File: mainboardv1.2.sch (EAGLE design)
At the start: 128 parts, among them IC1 LM2596S, IC2 TDA2822D, IC3 MCP2562P, IC4 STM32F103RBT6, IC5 MIC2288YD5, IC6 ULN2003AD, IC7 LM2901, IC8 REG1117, IC9 SN74LVC1G10, Q1 8MHz

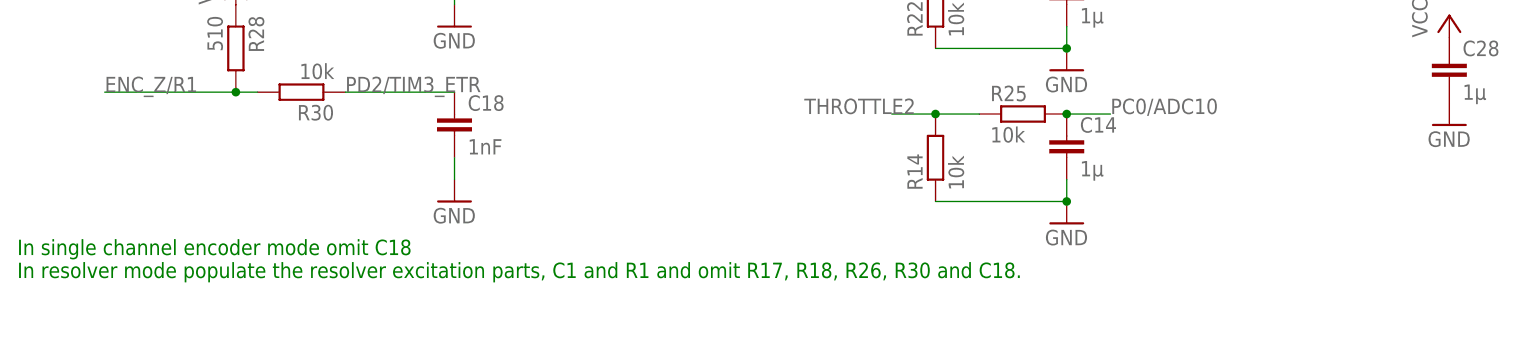
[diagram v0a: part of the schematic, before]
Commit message: Small changed for compatibility with JLCPCBs parts library
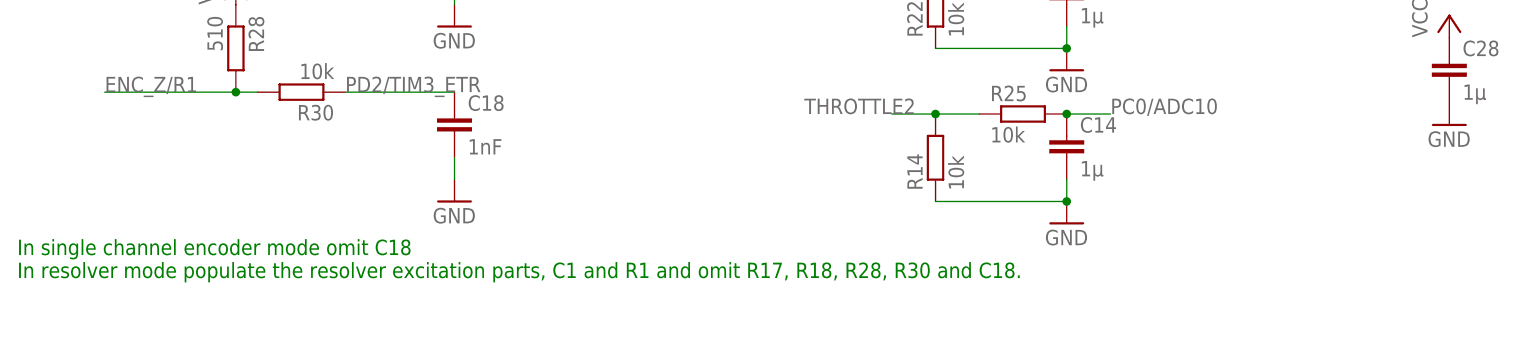
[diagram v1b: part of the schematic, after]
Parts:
- L4: device rcl:L-EUL2012C -> rcl:L-EUL2825P
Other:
- note added: "In single channel encoder mode omit C18 In resolver mode populate the resolver excitation parts, C1 and R1 and omit R17, R18, R28, R30 and C18."
- note removed: "In single channel encoder mode omit C18 In resolver mode populate the resolver excitation parts, C1 and R1 and omit R17, R18, R26, R30 and C18."
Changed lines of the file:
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@@
 <grid distance="0.1" unitdist="inch" unit="inch" style="lines" multiple="1" display="no" altdistance="0.01" altunitdist="inch" altunit="inch"/>
 <layers>
-<layer number="1" name="Top" color="12" fill="1" visible="no" active="no"/>
-<layer number="16" name="Bottom" color="1" fill="1" visible="no" active="no"/>
-<layer number="17" name="Pads" color="2" fill="1" visible="no" active="no"/>
-<layer number="18" name="Vias" color="2" fill="1" visible="no" active="no"/>
-<layer number="19" name="Unrouted" color="15" fill="1" visible="no" active="no"/>
-<layer number="20" name="Dimension" color="15" fill="1" visible="no" active="no"/>
-<layer number="21" name="tPlace" color="7" fill="1" visible="no" active="no"/>
-<layer number="22" name="bPlace" color="7" fill="1" visible="no" active="no"/>
-<layer number="23" name="tOrigins" color="15" fill="1" visible="no" active="no"/>
-<layer number="24" name="bOrigins" color="15" fill="1" visible="no" active="no"/>
-<layer number="25" name="tNames" color="7" fill="1" visible="no" active="no"/>
-<layer number="26" name="bNames" color="7" fill="1" visible="no" active="no"/>
-<layer number="27" name="tValues" color="7" fill="1" visible="no" active="no"/>
-<layer number="28" name="bValues" color="7" fill="1" visible="no" active="no"/>
+<layer number="1" name="Top" color="12" fill="1" visible="yes" active="no"/>
+<layer number="16" name="Bottom" color="1" fill="1" visible="yes" active="no"/>
+<layer number="17" name="Pads" color="2" fill="1" visible="yes" active="no"/>
+<layer number="18" name="Vias" color="2" fill="1" visible="yes" active="no"/>
+<layer number="19" name="Unrouted" color="15" fill="1" visible="yes" active="no"/>
+<layer number="20" name="Dimension" color="15" fill="1" visible="yes" active="no"/>
+<layer number="21" name="tPlace" color="7" fill="1" visible="yes" active="no"/>
+<layer number="22" name="bPlace" color="7" fill="1" visible="yes" active="no"/>
+<layer number="23" name="tOrigins" color="15" fill="1" visible="yes" active="no"/>
+<layer number="24" name="bOrigins" color="15" fill="1" visible="yes" active="no"/>
+<layer number="25" name="tNames" color="7" fill="1" visible="yes" active="no"/>
+<layer number="26" name="bNames" color="7" fill="1" visible="yes" active="no"/>
+<layer number="27" name="tValues" color="7" fill="1" visible="yes" active="no"/>
+<layer number="28" name="bValues" color="7" fill="1" visible="yes" active="no"/>
 <layer number="29" name="tStop" color="7" fill="3" visible="no" active="no"/>
 <layer number="30" name="bStop" color="7" fill="6" visible="no" active="no"/>
@@
 <layer number="35" name="tGlue" color="7" fill="4" visible="no" active="no"/>
 <layer number="36" name="bGlue" color="7" fill="5" visible="no" active="no"/>
-<layer number="37" name="tTest" color="7" fill="1" visible="no" active="no"/>
-<layer number="38" name="bTest" color="7" fill="1" visible="no" active="no"/>
+<layer number="37" name="tTest" color="7" fill="1" visible="yes" active="no"/>
+<layer number="38" name="bTest" color="7" fill="1" visible="yes" active="no"/>
 <layer number="39" name="tKeepout" color="4" fill="11" visible="no" active="no"/>
 <layer number="40" name="bKeepout" color="1" fill="11" visible="no" active="no"/>
@@
 <layer number="44" name="Drills" color="7" fill="1" visible="no" active="no"/>
 <layer number="45" name="Holes" color="7" fill="1" visible="no" active="no"/>
-<layer number="46" name="Milling" color="3" fill="1" visible="no" active="no"/>
-<layer number="47" name="Measures" color="7" fill="1" visible="no" active="no"/>
-<layer number="48" name="Document" color="7" fill="1" visible="no" active="no"/>
-<layer number="49" name="Reference" color="7" fill="1" visible="no" active="no"/>
-<layer number="50" name="dxf" color="7" fill="1" visible="no" active="no"/>
-<layer number="51" name="tDocu" color="7" fill="1" visible="no" active="no"/>
-<layer number="52" name="bDocu" color="7" fill="1" visible="no" active="no"/>
-<layer number="53" name="tGND_GNDA" color="7" fill="9" visible="no" active="no"/>
-<layer number="54" name="bGND_GNDA" color="1" fill="9" visible="no" active="no"/>
-<layer number="56" name="wert" color="7" fill="1" visible="no" active="no"/>
-<layer number="57" name="tCAD" color="7" fill="1" visible="no" active="no"/>
+<layer number="46" name="Milling" color="3" fill="1" visible="yes" active="no"/>
+<layer number="47" name="Measures" color="7" fill="1" visible="yes" active="no"/>
+<layer number="48" name="Document" color="7" fill="1" visible="yes" active="no"/>
+<layer number="49" name="Reference" color="7" fill="1" visible="yes" active="no"/>
+<layer number="50" name="dxf" color="7" fill="1" visible="yes" active="no"/>
+<layer number="51" name="tDocu" color="7" fill="1" visible="yes" active="no"/>
+<layer number="52" name="bDocu" color="7" fill="1" visible="yes" active="no"/>
+<layer number="53" name="tGND_GNDA" color="7" fill="9" visible="yes" active="no"/>
+<layer number="54" name="bGND_GNDA" color="1" fill="9" visible="yes" active="no"/>
+<layer number="56" name="wert" color="7" fill="1" visible="yes" active="no"/>
+<layer number="57" name="tCAD" color="7" fill="1" visible="yes" active="no"/>
 <layer number="91" name="Nets" color="2" fill="1" visible="yes" active="yes"/>
 <layer number="92" name="Busses" color="1" fill="1" visible="yes" active="yes"/>
@@
 <part name="IC5" library="adafruit" deviceset="MIC2288" device="YD5" value="MIC2288YD5"/>
 <part name="GND64" library="supply1" deviceset="GND" device=""/>
-<part name="L4" library="rcl" deviceset="L-EU" device="L2012C" value="10µH"/>
+<part name="L4" library="rcl" deviceset="L-EU" device="L2825P" value="10µH"/>
 <part name="R35" library="rcl" deviceset="R-EU_" device="R0603" value="3k3"/>
 <part name="R36" library="rcl" deviceset="R-EU_" device="R0603" value="510"/>
@@
 <text x="134.62" y="30.48" size="3.81" layer="92">Over Current Protection &amp; HW Shutdown</text>
 <text x="-165.1" y="-110.49" size="1.778" layer="91">In single channel encoder mode omit C18
-In resolver mode populate the resolver excitation parts, C1 and R1 and omit R17, R18, R26, R30 and C18.</text>
+In resolver mode populate the resolver excitation parts, C1 and R1 and omit R17, R18, R28, R30 and C18.</text>
 <text x="175.26" y="-78.74" size="1.778" layer="91">R2 connected to GND</text>
 <text x="-104.14" y="73.66" size="1.778" layer="91">Populate C1 and R1 only for resolver mode.

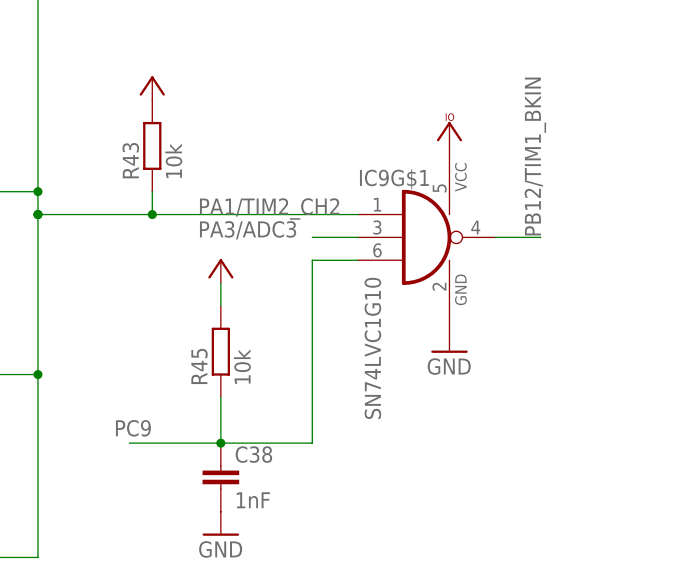
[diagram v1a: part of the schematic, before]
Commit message: Replaced SOT23-6 by SC70-6 foot print for IC9 Moved copyright info away from trace fixed font of silk screen
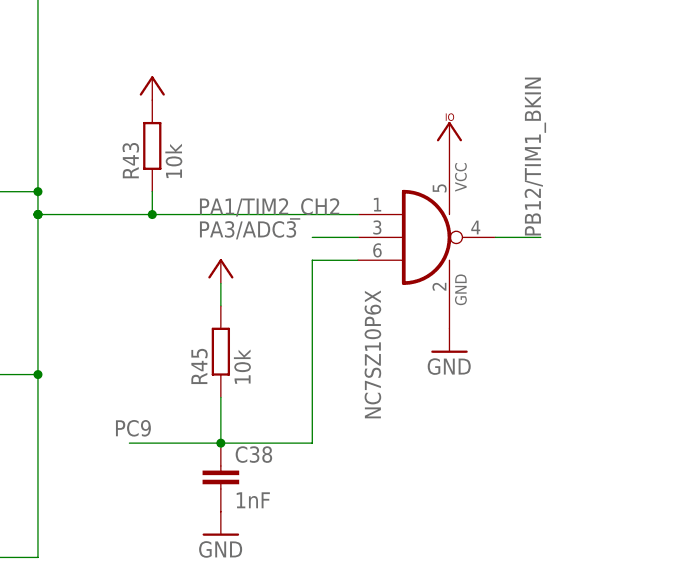
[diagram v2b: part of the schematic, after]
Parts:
- IC9: value SN74LVC1G10 -> NC7SZ10P6X; device 74xx-eu:741G10 -> 74xx-eu:741G10X
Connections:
- net GND: now also IC9PWR.GND; no longer IC9G$2.GND
- net PA1/TIM2_CH2: now also IC9>NAME.I0; no longer IC9G$1.I0
- net PA3/ADC3: now also IC9>NAME.I1; no longer IC9G$1.I1
- net PB12/TIM1_BKIN: now also IC9>NAME.O; no longer IC9G$1.O
- net PC9: now also IC9>NAME.I2; no longer IC9G$1.I2
- net VCCIO: now also IC9PWR.VCC; no longer IC9G$2.VCC
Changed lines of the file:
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@@
 <part name="GND45" library="supply1" deviceset="GND" device=""/>
 <part name="P+15" library="supply1" deviceset="VCC" device=""/>
-<part name="IC9" library="74xx-eu" deviceset="74*1G10" device="" value="SN74LVC1G10"/>
 <part name="GND17" library="supply1" deviceset="GND" device=""/>
 <part name="VCC4" library="supply1" deviceset="VCCIO" device=""/>
@@
 <part name="LOGO1" library="SparkFun-Aesthetics" deviceset="OSHW-LOGO" device="M"/>
 <part name="SJ1" library="SparkFun-Passives" deviceset="SOLDERJUMPER" device="TRACE"/>
+<part name="IC9" library="74xx-eu" deviceset="74*1G10" device="X" value="NC7SZ10P6X"/>
 </parts>
 <sheets>
@@
 <instance part="GND45" gate="1" x="182.88" y="43.18"/>
 <instance part="P+15" gate="VCC" x="-38.1" y="-40.64"/>
-<instance part="IC9" gate="G$1" x="246.38" y="-5.08" smashed="yes">
-<attribute name="NAME" x="238.76" y="0.635" size="1.778" layer="95"/>
-<attribute name="VALUE" x="241.3" y="-25.4" size="1.778" layer="96" rot="R90"/>
-</instance>
-<instance part="IC9" gate="G$2" x="248.92" y="-5.08" smashed="yes"/>
 <instance part="GND17" gate="1" x="248.92" y="-17.78"/>
 <instance part="VCC4" gate="G$1" x="248.92" y="7.62" smashed="yes"/>
@@
 <instance part="LOGO1" gate="G$1" x="-45.72" y="60.96"/>
 <instance part="SJ1" gate="1" x="-81.28" y="106.68"/>
+<instance part="IC9" gate="&gt;NAME" x="246.38" y="-5.08" smashed="yes">
+<attribute name="VALUE" x="241.3" y="-25.4" size="1.778" layer="96" rot="R90"/>
+</instance>
+<instance part="IC9" gate="PWR" x="248.92" y="-5.08" smashed="yes"/>
 </instances>
 <busses>
@@
 <wire x1="254" y1="-5.08" x2="259.08" y2="-5.08" width="0.1524" layer="91"/>
 <label x="259.08" y="-5.08" size="1.778" layer="95" rot="R90"/>
-<pinref part="IC9" gate="G$1" pin="O"/>
+<pinref part="IC9" gate="&gt;NAME" pin="O"/>
 </segment>
 </net>
@@
 <pinref part="C38" gate="G$1" pin="1"/>
 <wire x1="223.52" y1="-22.86" x2="223.52" y2="-27.94" width="0.1524" layer="91"/>
-<pinref part="IC9" gate="G$1" pin="I2"/>
 <label x="215.9" y="-25.4" size="1.778" layer="95" rot="R180"/>
 <wire x1="238.76" y1="-7.62" x2="233.68" y2="-7.62" width="0.1524" layer="91"/>
@@
 <junction x="223.52" y="-27.94"/>
 <wire x1="223.52" y1="-27.94" x2="213.36" y2="-27.94" width="0.1524" layer="91"/>
+<pinref part="IC9" gate="&gt;NAME" pin="I2"/>
 </segment>
 <segment>
@@
 </segment>
 <segment>
-<pinref part="IC9" gate="G$2" pin="GND"/>
-<pinref part="GND17" gate="1" pin="GND"/>
-</segment>
-<segment>
 <pinref part="GND46" gate="1" pin="GND"/>
 <pinref part="C26" gate="G$1" pin="2"/>
@@
 <pinref part="GND4" gate="1" pin="GND"/>
 <pinref part="C48" gate="G$1" pin="2"/>
+</segment>
+<segment>
+<pinref part="GND17" gate="1" pin="GND"/>
+<pinref part="IC9" gate="PWR" pin="GND"/>
 </segment>
 </net>
@@
 <wire x1="215.9" y1="0" x2="215.9" y2="-2.54" width="0.1524" layer="91"/>
 <wire x1="215.9" y1="-2.54" x2="238.76" y2="-2.54" width="0.1524" layer="91"/>
-<pinref part="IC9" gate="G$1" pin="I0"/>
 <wire x1="193.04" y1="0" x2="203.2" y2="0" width="0.1524" layer="91"/>
 <junction x="203.2" y="0"/>
 <wire x1="215.9" y1="-2.54" x2="203.2" y2="-2.54" width="0.1524" layer="91"/>
 <junction x="215.9" y="-2.54"/>
+<pinref part="IC9" gate="&gt;NAME" pin="I0"/>
 </segment>
 </net>
@@
 <wire x1="238.76" y1="-5.08" x2="233.68" y2="-5.08" width="0.1524" layer="91"/>
 <label x="220.98" y="-5.08" size="1.778" layer="95"/>
-<pinref part="IC9" gate="G$1" pin="I1"/>
+<pinref part="IC9" gate="&gt;NAME" pin="I1"/>
 </segment>
 </net>
@@
 </segment>
 <segment>
-<pinref part="IC9" gate="G$2" pin="VCC"/>
 <pinref part="VCC4" gate="G$1" pin="VCCIO"/>
-</segment>
-</net>
+<pinref part="IC9" gate="PWR" pin="VCC"/>
+</segment>
+</net>
